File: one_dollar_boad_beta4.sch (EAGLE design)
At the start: 39 parts, among them IC1 ATTINY85, X1 USBPCB

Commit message: Modificação feita por Marcelo Cuin
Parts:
- CONNECTORBAR1: value FAMALEBAR01X08 -> .
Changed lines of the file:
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@@
 <?xml version="1.0" encoding="utf-8"?>
 <!DOCTYPE eagle SYSTEM "eagle.dtd">
-<eagle version="7.5.0">
+<eagle version="7.2.0">
 <drawing>
 <settings>
@@
 <part name="J7" library="con-amp" deviceset="MTA02-100" device=""/>
 <part name="J8" library="con-amp" deviceset="MTA02-100" device=""/>
-<part name="CONNECTORBAR1" library="femeabarra01x08" deviceset="FAMALEBAR01X08" device=""/>
+<part name="CONNECTORBAR1" library="femeabarra01x08" deviceset="FAMALEBAR01X08" device="" value="."/>
 <part name="U$9" library="arduinopinagem" deviceset="ARDUINOPINAGEM" device=""/>
 <part name="ICSP1" library="ICSP" deviceset="ICSP" device=""/>

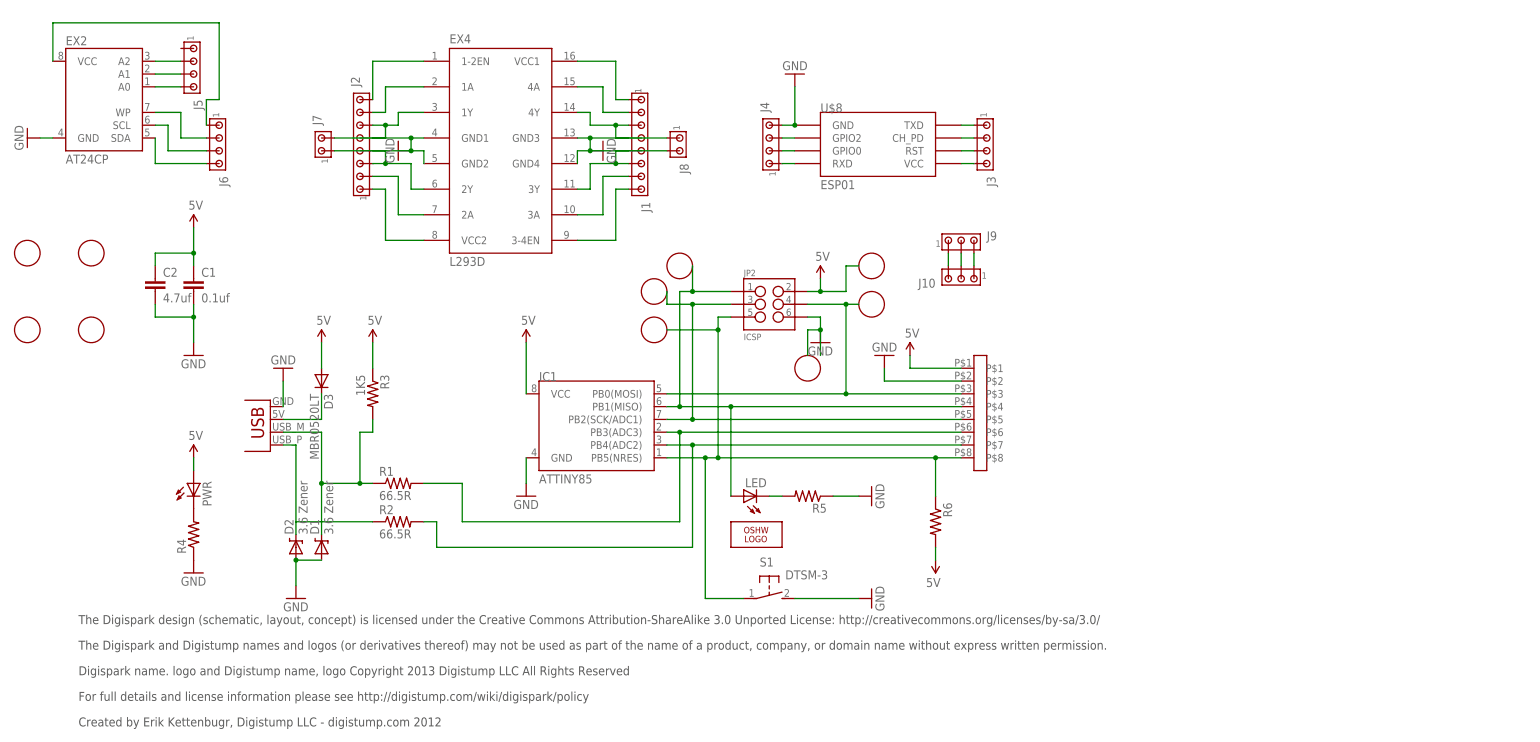
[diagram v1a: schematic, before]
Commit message: Nome adicionado One Dollar Board Beta 4
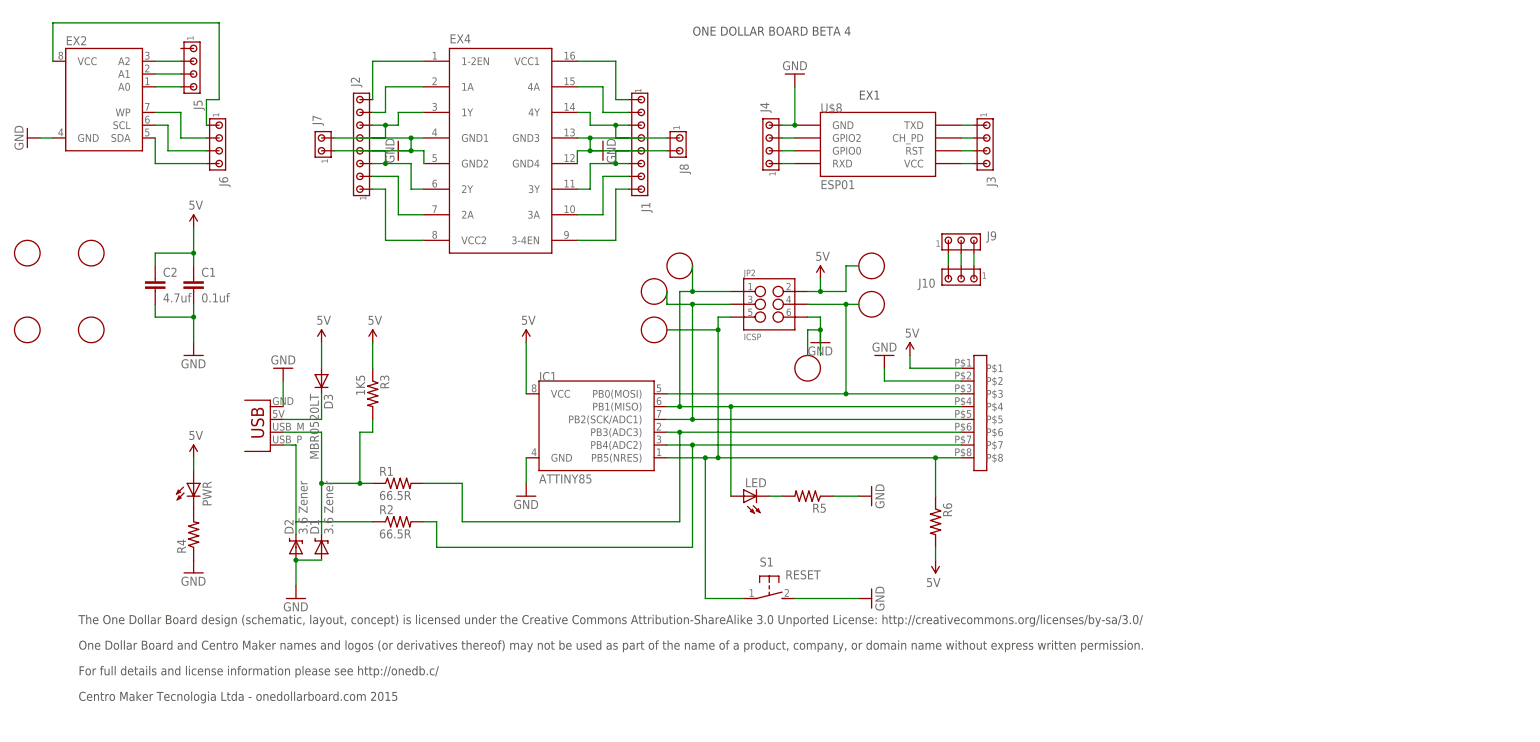
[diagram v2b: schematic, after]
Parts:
- removed LOGO2: LOGO-OSHW-10MILX0200-NT, logo:LOGO-OSHW-10MILX0200-NT
- S1: value DTSM-3 -> RESET
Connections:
- net N$22 renamed EX1
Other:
- note added: "Centro Maker Tecnologia Ltda - onedollarboard.com 2015"
- note added: "EX1"
- note added: "For full details and license information please see http://onedb.c/"
- note added: "ONE DOLLAR BOARD BETA 4"
- note added: "One Dollar Board and Centro Maker names and logos (or derivatives thereof) may not be used as part of the name of a product, company, or domain name without express written permission."
- note added: "The One Dollar Board design (schematic, layout, concept) is licensed under the Creative Commons Attribution-ShareAlike 3.0 Unported License: http://creativecommons.org/licenses/by-sa/3.0/"
- note removed: "Created by Erik Kettenbugr, Digistump LLC - digistump.com 2012"
- note removed: "Digispark name. logo and Digistump name, logo Copyright 2013 Digistump LLC All Rights Reserved"
- note removed: "For full details and license information please see http://digistump.com/wiki/digispark/policy"
- note removed: "The Digispark and Digistump names and logos (or derivatives thereof) may not be used as part of the name of a product, company, or domain name without express written permission."
- note removed: "The Digispark design (schematic, layout, concept) is licensed under the Creative Commons Attribution-ShareAlike 3.0 Unported License: http://creativecommons.org/licenses/by-sa/3.0/"
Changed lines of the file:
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@@
 <?xml version="1.0" encoding="utf-8"?>
 <!DOCTYPE eagle SYSTEM "eagle.dtd">
-<eagle version="7.2.0">
+<eagle version="6.6.0">
 <drawing>
 <settings>
@@
 <part name="GND13" library="SparkFun" deviceset="GND" device=""/>
 <part name="C2" library="SparkFun" deviceset="CAP" device="0805" value="4.7uf"/>
-<part name="LOGO2" library="logo" deviceset="LOGO-OSHW-10MIL" device="X0200-NT"/>
 <part name="U$4" library="SparkFun" deviceset="5V" device=""/>
 <part name="GND4" library="SparkFun" deviceset="GND" device=""/>
@@
 <part name="GND5" library="SparkFun" deviceset="GND" device=""/>
 <part name="U$6" library="SparkFun" deviceset="5V" device=""/>
-<part name="S1" library="switch-tact" deviceset="DTSM-3" device=""/>
+<part name="S1" library="switch-tact" deviceset="DTSM-3" device="" value="RESET"/>
 <part name="GND7" library="SparkFun" deviceset="GND" device=""/>
-<part name="EX4" library="st-microelectronics" deviceset="L293D" device=""/>
+<part name="EX4" library="st-microelectronics" deviceset="L293D" device="" value=""/>
 <part name="J1" library="con-amp" deviceset="MTA08-100" device=""/>
 <part name="J2" library="con-amp" deviceset="MTA08-100" device=""/>
@@
 <part name="J3" library="con-amp" deviceset="MTA04-100" device=""/>
 <part name="J4" library="con-amp" deviceset="MTA04-100" device=""/>
-<part name="EX2" library="atmel" deviceset="AT24C*" device="P"/>
+<part name="EX2" library="atmel" deviceset="AT24C*" device="P" value=""/>
 <part name="GND8" library="supply1" deviceset="GND" device=""/>
 <part name="GND9" library="SparkFun" deviceset="GND" device=""/>
@@
 <sheet>
 <plain>
-<text x="-43.18" y="0" size="1.778" layer="97">The Digispark design (schematic, layout, concept) is licensed under the Creative Commons Attribution-ShareAlike 3.0 Unported License: http://creativecommons.org/licenses/by-sa/3.0/</text>
-<text x="-43.18" y="-5.08" size="1.778" layer="97">The Digispark and Digistump names and logos (or derivatives thereof) may not be used as part of the name of a product, company, or domain name without express written permission.</text>
-<text x="-43.18" y="-10.16" size="1.778" layer="97">Digispark name. logo and Digistump name, logo Copyright 2013 Digistump LLC All Rights Reserved</text>
-<text x="-43.18" y="-15.24" size="1.778" layer="97">For full details and license information please see http://digistump.com/wiki/digispark/policy</text>
-<text x="-43.18" y="-20.32" size="1.778" layer="97">Created by Erik Kettenbugr, Digistump LLC - digistump.com 2012</text>
+<text x="-43.18" y="0" size="1.778" layer="97">The One Dollar Board design (schematic, layout, concept) is licensed under the Creative Commons Attribution-ShareAlike 3.0 Unported License: http://creativecommons.org/licenses/by-sa/3.0/</text>
+<text x="-43.18" y="-5.08" size="1.778" layer="97">One Dollar Board and Centro Maker names and logos (or derivatives thereof) may not be used as part of the name of a product, company, or domain name without express written permission.</text>
+<text x="-43.18" y="-10.16" size="1.778" layer="97">For full details and license information please see http://onedb.c/</text>
+<text x="-43.18" y="-15.24" size="1.778" layer="97">Centro Maker Tecnologia Ltda - onedollarboard.com 2015</text>
+<text x="78.74" y="116.84" size="1.778" layer="97">ONE DOLLAR BOARD BETA 4</text>
+<text x="111.76" y="104.14" size="1.778" layer="97">EX1</text>
 </plain>
 <instances>
@@
 <instance part="GND13" gate="1" x="-20.32" y="53.34"/>
 <instance part="C2" gate="G$1" x="-27.94" y="66.04"/>
-<instance part="LOGO2" gate="G$1" x="91.44" y="17.78"/>
 <instance part="U$4" gate="G$1" x="121.92" y="53.34"/>
 <instance part="GND4" gate="1" x="116.84" y="53.34" rot="R180"/>
@@
 </segment>
 </net>
-<net name="N$22" class="0">
+<net name="EX1" class="0">
 <segment>
 <pinref part="EX4" gate="G$1" pin="4A"/>

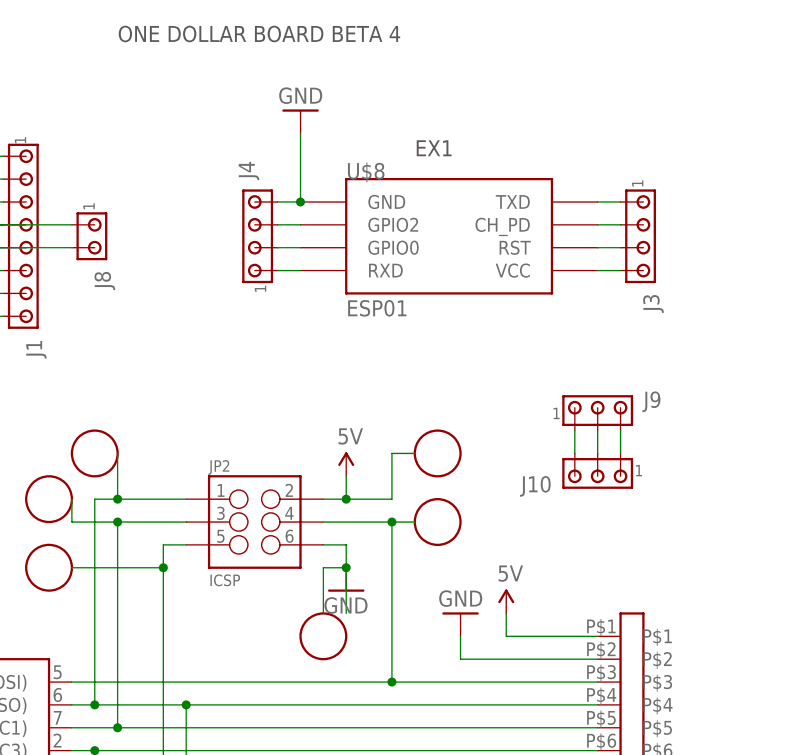
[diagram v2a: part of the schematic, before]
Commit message: Adicionado nome de pinos e mudança de lugar de RST
Colocado números e descrição de PINOS
Mudança de lugar de Botão RESET
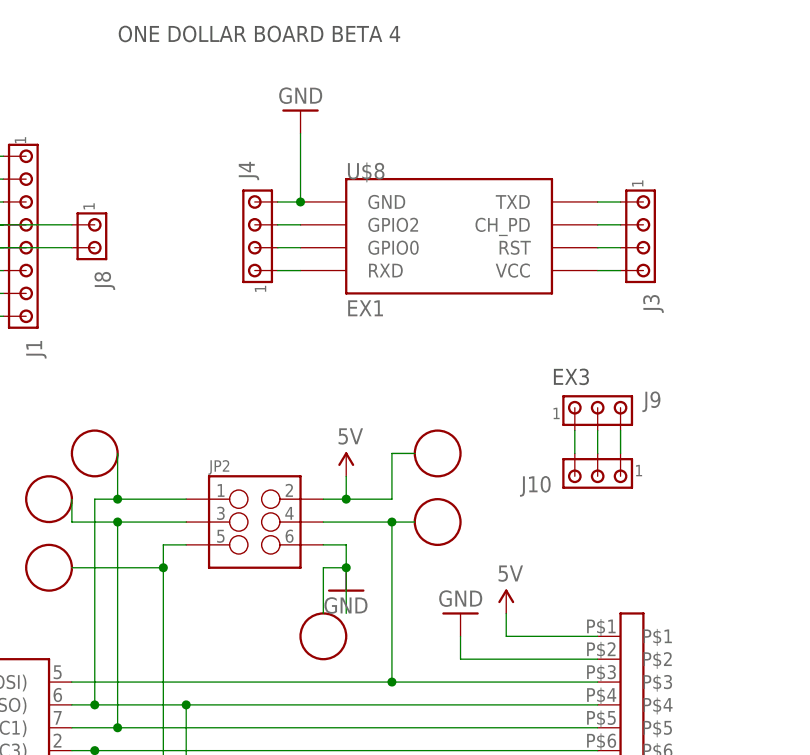
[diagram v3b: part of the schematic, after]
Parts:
- JP2: value ICSP -> (none)
- U$8: value ESP01 -> EX1
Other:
- note added: "EX3"
- note removed: "EX1"
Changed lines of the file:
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@@
 <part name="U$4" library="SparkFun" deviceset="5V" device=""/>
 <part name="GND4" library="SparkFun" deviceset="GND" device=""/>
-<part name="JP2" library="SparkFun-Connectors" deviceset="M03X2" device="2X3_SILK_MALE_PTH" value="ICSP"/>
+<part name="JP2" library="SparkFun-Connectors" deviceset="M03X2" device="2X3_SILK_MALE_PTH"/>
 <part name="GND5" library="SparkFun" deviceset="GND" device=""/>
 <part name="U$6" library="SparkFun" deviceset="5V" device=""/>
@@
 <part name="J1" library="con-amp" deviceset="MTA08-100" device=""/>
 <part name="J2" library="con-amp" deviceset="MTA08-100" device=""/>
-<part name="U$8" library="esp8266modules" deviceset="ESP01" device=""/>
+<part name="U$8" library="esp8266modules" deviceset="ESP01" device="" value="EX1"/>
 <part name="J3" library="con-amp" deviceset="MTA04-100" device=""/>
 <part name="J4" library="con-amp" deviceset="MTA04-100" device=""/>
@@
 <text x="-43.18" y="-15.24" size="1.778" layer="97">Centro Maker Tecnologia Ltda - onedollarboard.com 2015</text>
 <text x="78.74" y="116.84" size="1.778" layer="97">ONE DOLLAR BOARD BETA 4</text>
-<text x="111.76" y="104.14" size="1.778" layer="97">EX1</text>
+<text x="127" y="78.74" size="1.778" layer="97">EX3</text>
 </plain>
 <instances>
